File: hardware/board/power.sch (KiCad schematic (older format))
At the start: 21 parts, among them J1 POWER, SW1 POWER, U1 LD1117-3.3

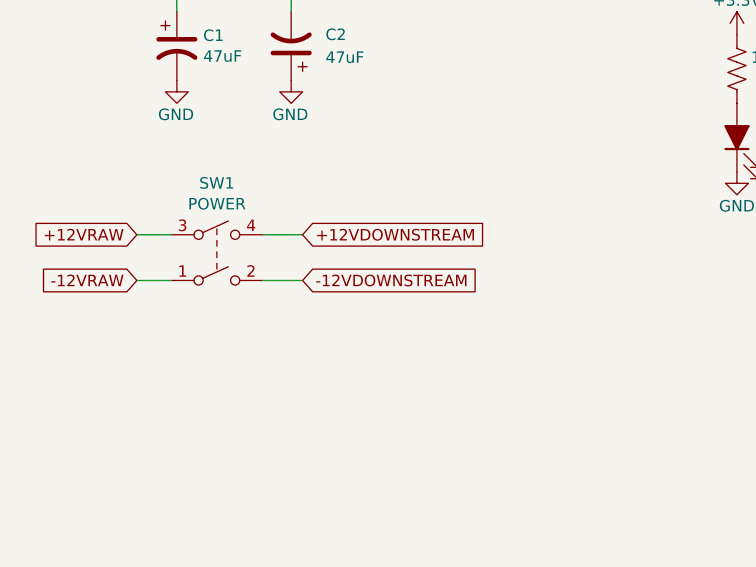
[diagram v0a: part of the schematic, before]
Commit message: More updates to the board design
- Added polyfuses for downstream power
- Added breakout header for external, panel-mounted USB port
- Added I/O breakout for the switches and buttons on the front control panel
- Made the MCU footprint a hybrid QFP/QFN footprint
- Add a nice illustration to the board backside
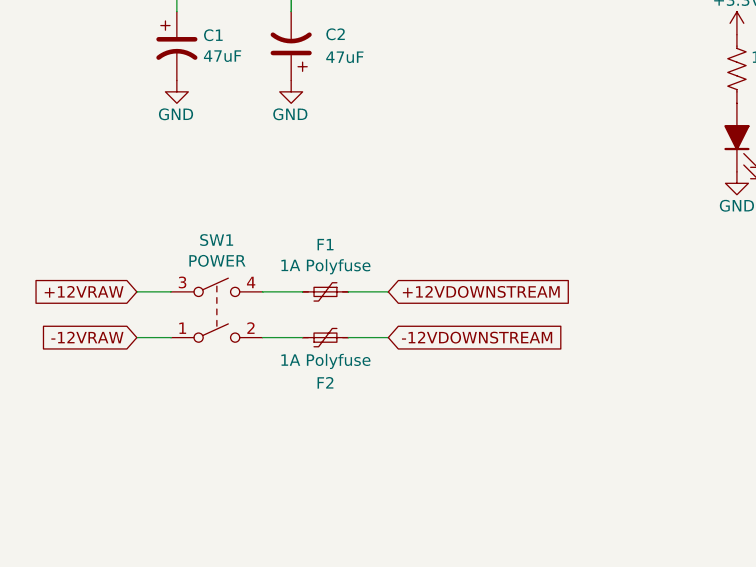
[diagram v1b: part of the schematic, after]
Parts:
- added F1, F2: 1A Polyfuse, winterbloom:Littelfuse_0805L, symbol Device:Polyfuse_Small
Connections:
- net +12VDOWNSTREAM: now also F1.1; no longer SW1.4
- net -12VDOWNSTREAM: now also F2.2; no longer SW1.2
- new net: F2.1, SW1.2
- new net: F1.2, SW1.4
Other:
- moved on the sheet: SW1
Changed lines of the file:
@@
 Sheet 2 7
 Title "Hubble Motherboard"
-Date "2021-11-12"
+Date "2021-11-20"
 Rev "v2"
 Comp "Winterbloom"
 Comment1 "Alethea Flowers"
 Comment2 "CERN-OHL-P V2"
-Comment3 ""
+Comment3 "hubble.wntr.dev"
 Comment4 ""
 $EndDescr
@@
 +12VRAW
 Wire Wire Line
-	1075 3325 1225 3325
-Wire Wire Line
-	1075 3125 1225 3125
+	1075 3575 1225 3575
+Wire Wire Line
+	1075 3375 1225 3375
 $Comp
 L power:+12V #PWR011
@@
 L Switch:SW_DPST SW1
 U 1 1 60721796
-P 1425 3225
-F 0 "SW1" H 1425 3550 50  0000 C CNN
-F 1 "POWER" H 1425 3459 50  0000 C CNN
-F 2 "Connector_Wire:SolderWire-0.75sqmm_1x04_P4.8mm_D1.25mm_OD2.3mm" H 1425 3225 50  0001 C CNN
-F 3 "~" H 1425 3225 50  0001 C CNN
-	1    1425 3225
-	1    0    0    -1
-$EndComp
-Text GLabel 1800 3125 2    50   Input ~ 0
+P 1425 3475
+F 0 "SW1" H 1425 3800 50  0000 C CNN
+F 1 "POWER" H 1425 3709 50  0000 C CNN
+F 2 "Connector_Wire:SolderWire-0.75sqmm_1x04_P4.8mm_D1.25mm_OD2.3mm" H 1425 3475 50  0001 C CNN
+F 3 "~" H 1425 3475 50  0001 C CNN
+	1    1425 3475
+	1    0    0    -1
+$EndComp
+Text GLabel 2175 3375 2    50   Input ~ 0
 +12VDOWNSTREAM
-Text GLabel 1800 3325 2    50   Input ~ 0
+Text GLabel 2175 3575 2    50   Input ~ 0
 -12VDOWNSTREAM
 Wire Wire Line
-	1800 3125 1625 3125
-Wire Wire Line
-	1625 3325 1800 3325
+	1800 3375 1625 3375
+Wire Wire Line
+	1625 3575 1800 3575
 $Comp
 L Device:CP1 C1
@@
 	1    0    0    -1
 $EndComp
-Text GLabel 1075 3325 0    50   Input ~ 0
+Text GLabel 1075 3575 0    50   Input ~ 0
 -12VRAW
-Text GLabel 1075 3125 0    50   Input ~ 0
+Text GLabel 1075 3375 0    50   Input ~ 0
 +12VRAW
 $Comp
@@
 	1    0    0    -1
 $EndComp
+$Comp
+L Device:Polyfuse_Small F2
+U 1 1 619A3015
+P 1900 3575
+F 0 "F2" V 1700 3575 50  0000 C CNN
+F 1 "1A Polyfuse" V 1800 3575 50  0000 C CNN
+F 2 "winterbloom:Littelfuse_0805L" H 1950 3375 50  0001 L CNN
+F 3 "https://m.littelfuse.com/~/media/electronics/datasheets/resettable_ptcs/littelfuse_ptc_0805l_datasheet.pdf.pdf" H 1900 3575 50  0001 C CNN
+F 4 "0805L075" V 1900 3575 50  0001 C CNN "mpn"
+	1    1900 3575
+	0    -1   -1   0
+$EndComp
+$Comp
+L Device:Polyfuse_Small F1
+U 1 1 619A193A
+P 1900 3375
+F 0 "F1" V 1695 3375 50  0000 C CNN
+F 1 "1A Polyfuse" V 1786 3375 50  0000 C CNN
+F 2 "winterbloom:Littelfuse_0805L" H 1950 3175 50  0001 L CNN
+F 3 "https://m.littelfuse.com/~/media/electronics/datasheets/resettable_ptcs/littelfuse_ptc_0805l_datasheet.pdf.pdf" H 1900 3375 50  0001 C CNN
+F 4 "0805L075" V 1900 3375 50  0001 C CNN "mpn"
+	1    1900 3375
+	0    1    1    0
+$EndComp
+Wire Wire Line
+	2000 3375 2175 3375
+Wire Wire Line
+	2175 3575 2000 3575
 $EndSCHEMATC
